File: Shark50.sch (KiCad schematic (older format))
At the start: 24 parts, among them J1 USB_B_Mini, SW1 MXSwitch, SW2 MXSwitch, SW3 MXSwitch, SW4 MXSwitch, U1 ATmega32U4-AU, Y1 16MHz

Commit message: feat: added matrix first row
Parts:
- added D10, D11, D12, D13, D14, D5, D6, D7, D8, D9: 1N4148W, Diodes_SMD:D_SOD-123, symbol Device:D_Small
- added R5: 330, Resistors_SMD:R_1206_HandSoldering, symbol Device:R_Small
- added SW10: O, acheron_MX:MX100, symbol acheronSymbols:MXSwitch
- added SW11: P, acheron_MX:MX100, symbol acheronSymbols:MXSwitch
- added SW12: [, acheron_MX:MX100, symbol acheronSymbols:MXSwitch
- added SW13: ], acheron_MX:MX100, symbol acheronSymbols:MXSwitch
- added SW14: BkSpc, acheron_MX:MX100, symbol acheronSymbols:MXSwitch
- added SW5: R, acheron_MX:MX100, symbol acheronSymbols:MXSwitch
- added SW6: T, acheron_MX:MX100, symbol acheronSymbols:MXSwitch
- added SW7: Y, acheron_MX:MX100, symbol acheronSymbols:MXSwitch
- added SW8: U, acheron_MX:MX100, symbol acheronSymbols:MXSwitch
- added SW9: I, acheron_MX:MX100, symbol acheronSymbols:MXSwitch
- D1, D2, D3, D4: value D_Small -> 1N4148W
- R4: value 10k -> 1k
- SW1: value MXSwitch -> Esc
- SW2: value MXSwitch -> Q
- SW3: value MXSwitch -> W
- SW4: value MXSwitch -> E
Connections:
- net labels added: Col10, Col11, Col12, Col13, Col14, Col3, Col4, Col5, Col6, Col7, Col8, Col9
- wire segments 69 -> 125
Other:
- moved on the sheet: C1, C2, C3, C4, C5, C6, C7, C8, D1, D2, J1, R1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

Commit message: feat: matrix ready
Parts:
- added D? (x31): 1N4148W, Diodes_SMD:D_SOD-123, symbol Device:D_Small
- added SW?: Tab, acheron_MX:MX100, symbol acheronSymbols:MXSwitch
- added SW?: A, acheron_MX:MX100, symbol acheronSymbols:MXSwitch
- added SW?: S, acheron_MX:MX100, symbol acheronSymbols:MXSwitch
- added SW?: D, acheron_MX:MX100, symbol acheronSymbols:MXSwitch
- added SW?: F, acheron_MX:MX100, symbol acheronSymbols:MXSwitch
- added SW?: G, acheron_MX:MX100, symbol acheronSymbols:MXSwitch
- added SW?: H, acheron_MX:MX100, symbol acheronSymbols:MXSwitch
- added SW?: J, acheron_MX:MX100, symbol acheronSymbols:MXSwitch
- added SW?: K, acheron_MX:MX100, symbol acheronSymbols:MXSwitch
- added SW?: L, acheron_MX:MX100, symbol acheronSymbols:MXSwitch
- added SW?: ;, acheron_MX:MX100, symbol acheronSymbols:MXSwitch
- added SW?: ', acheron_MX:MX100, symbol acheronSymbols:MXSwitch
- added SW?: Enter, acheron_MX:MX100, symbol acheronSymbols:MXSwitch
- added SW?: LShift, acheron_MX:MX100, symbol acheronSymbols:MXSwitch
- added SW?: Z, acheron_MX:MX100, symbol acheronSymbols:MXSwitch
- added SW?: X, acheron_MX:MX100, symbol acheronSymbols:MXSwitch
- added SW?: C, acheron_MX:MX100, symbol acheronSymbols:MXSwitch
- added SW?: V, acheron_MX:MX100, symbol acheronSymbols:MXSwitch
- added SW?: B, acheron_MX:MX100, symbol acheronSymbols:MXSwitch
- added SW?: N, acheron_MX:MX100, symbol acheronSymbols:MXSwitch
- added SW?: M, acheron_MX:MX100, symbol acheronSymbols:MXSwitch
- added SW?: <, acheron_MX:MX100, symbol acheronSymbols:MXSwitch
- added SW?: >, acheron_MX:MX100, symbol acheronSymbols:MXSwitch
- added SW?: /, acheron_MX:MX100, symbol acheronSymbols:MXSwitch
- added SW?: RShift, acheron_MX:MX100, symbol acheronSymbols:MXSwitch
- added SW?: Fn, acheron_MX:MX100, symbol acheronSymbols:MXSwitch
- added SW?: LCtrl, acheron_MX:MX100, symbol acheronSymbols:MXSwitch
- added SW?: LAlt, acheron_MX:MX100, symbol acheronSymbols:MXSwitch
- added SW?: Space, acheron_MX:MX100, symbol acheronSymbols:MXSwitch
- added SW?: RAlt, acheron_MX:MX100, symbol acheronSymbols:MXSwitch
- added SW?: RCtr, acheron_MX:MX100, symbol acheronSymbols:MXSwitch
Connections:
- net labels added: Row3, Row4
- wire segments 125 -> 235
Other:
- moved on the sheet: D8, SW1, SW8

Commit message: feat: matrix symbols
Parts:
- SW15: renamed from SW?; value Tab -> Tab_125; footprint acheron_MX:MX100 -> acheron_MX:MX125
- SW17: renamed from SW?; value LCtrl -> LCtrl_125; footprint acheron_MX:MX100 -> acheron_MX:MX125
- SW22: renamed from SW?; value LAlt -> LAlt_125; footprint acheron_MX:MX100 -> acheron_MX:MX125
- SW29: renamed from SW?; value Space -> Space_7; footprint acheron_MX:MX100 -> acheron_MX:MX700
- SW40: renamed from SW?; value RAlt -> RAlt_125; footprint acheron_MX:MX100 -> acheron_MX:MX125
- SW42: renamed from SW?; value RShift -> RShift_125; footprint acheron_MX:MX100 -> acheron_MX:MX125
- SW43: renamed from SW?; value Enter -> Enter_175; footprint acheron_MX:MX100 -> acheron_MX:MX175
- SW45: renamed from SW?; value RCtr -> RCtr_125; footprint acheron_MX:MX100 -> acheron_MX:MX125
- gave numbers to parts that had none: 54

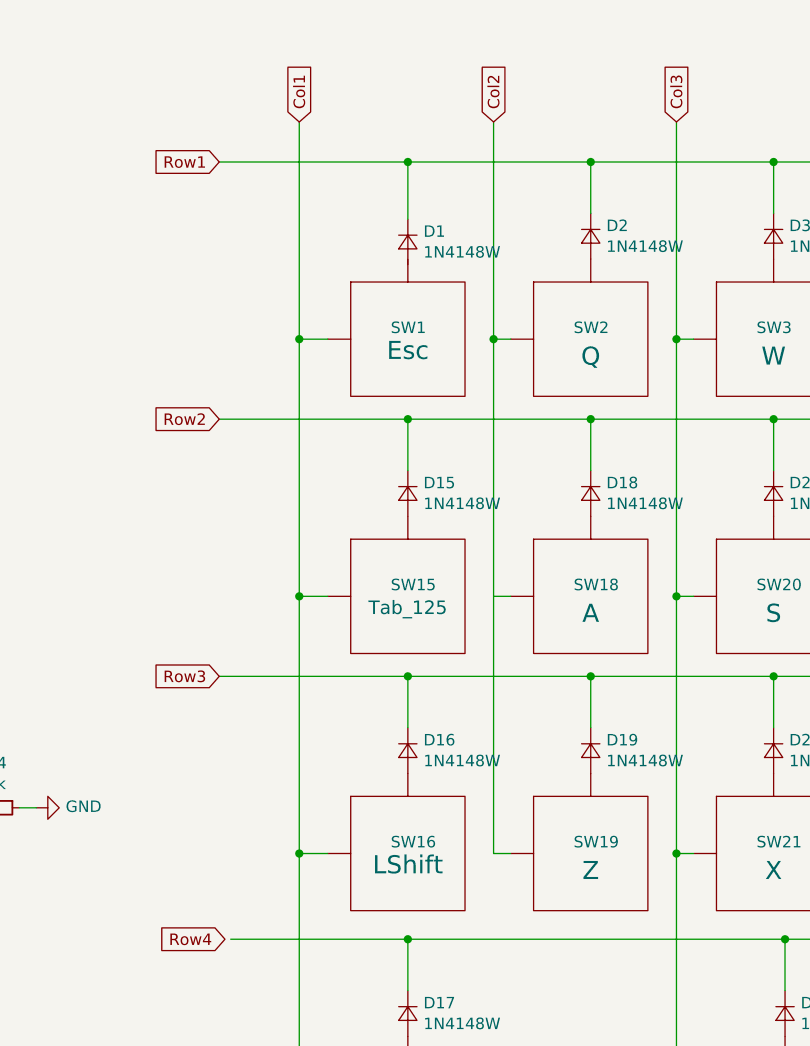
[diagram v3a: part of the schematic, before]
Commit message: feat: added switches layout to the PCB
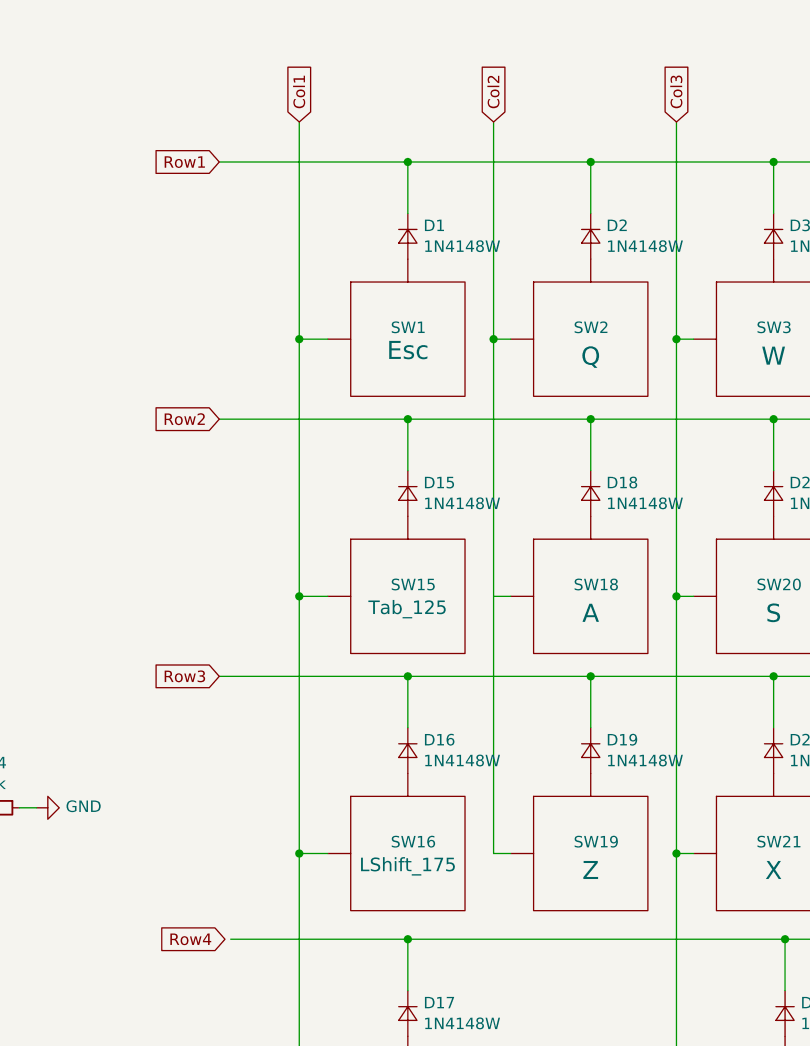
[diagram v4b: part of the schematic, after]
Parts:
- SW16: value LShift -> LShift_175; footprint acheron_MX:MX100 -> acheron_MX:MX175
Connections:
- net at SW1.2 (Row): now also D1.2 (A)
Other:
- moved on the sheet: D1
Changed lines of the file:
@@
 L Device:D_Small D1
 U 1 1 5D7299C3
-P 5825 1800
-F 0 "D1" V 5779 1868 50  0000 L CNN
-F 1 "1N4148W" V 5870 1868 50  0000 L CNN
-F 2 "Diodes_SMD:D_SOD-123" V 5825 1800 50  0001 C CNN
-F 3 "~" V 5825 1800 50  0001 C CNN
-	1    5825 1800
+P 5825 1775
+F 0 "D1" V 5779 1843 50  0000 L CNN
+F 1 "1N4148W" V 5870 1843 50  0000 L CNN
+F 2 "Diodes_SMD:D_SOD-123" V 5825 1775 50  0001 C CNN
+F 3 "~" V 5825 1775 50  0001 C CNN
+	1    5825 1775
 	0    1    1    0
 $EndComp
@@
 Wire Wire Line
 	6625 1675 6625 1450
-Wire Wire Line
-	5825 1700 5825 1450
 Wire Wire Line
 	6275 2225 6200 2225
@@
 Wire Wire Line
 	15825 1275 15825 2225
-Connection ~ 5825 1450
-Wire Wire Line
-	5825 1450 5000 1450
-Wire Wire Line
-	6625 1450 5825 1450
 Wire Wire Line
 	5350 1275 5350 2225
@@
 P 5825 4475
 F 0 "SW16" H 5750 4525 50  0000 L CNN
-F 1 "LShift" H 5825 4425 79  0000 C CNN
-F 2 "acheron_MX:MX100" H 5825 4475 50  0001 C CNN
+F 1 "LShift_175" H 5825 4425 59  0000 C CNN
+F 2 "acheron_MX:MX175" H 5825 4475 50  0001 C CNN
 F 3 "" H 5825 4475 50  0001 C CNN
 	1    5825 4475
@@
 Wire Wire Line
 	13425 4475 13425 5625
+Wire Wire Line
+	5000 1450 5825 1450
+Wire Wire Line
+	5825 1675 5825 1450
+Connection ~ 5825 1450
+Wire Wire Line
+	5825 1450 6625 1450
 $EndSCHEMATC
